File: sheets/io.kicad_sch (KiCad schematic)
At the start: 6 parts, among them Q5 BSS138, Q6 BSS138

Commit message: add mcu module + position components
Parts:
- removed Q5, Q6: BSS138, Package_TO_SOT_SMD:SOT-23, symbol Transistor_FET:BSS138
- added Q5, Q7: 2N7002, Package_TO_SOT_SMD:SOT-23, symbol Transistor_FET:2N7002
- added TB29, TB30: MKDSN 1,5/ 2-5,08, TerminalBlock_Phoenix:TerminalBlock_Phoenix_MKDS-1,5-2-5.08_1x02_P5.08mm_Horizontal, symbol Connector:Screw_Terminal_01x02
- renumbered R30 to R35, R31 to R36, R32 to R37, R33 to R38
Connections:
- net +3V3: now also Q5.1 (G), Q7.1 (G)
- net +5V: now also TB29.2 (Pin_2), TB30.1 (Pin_1), TB30.2 (Pin_2)
- net I2C.SCL: now also Q5.3 (D)
- net I2C.SDA: now also Q7.3 (D)
- net IO_SCL: now also Q5.2 (S)
- net IO_SDA: now also Q7.2 (S)
- new net +12V: TB29.1 (Pin_1)
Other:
- sheet Output PortC ports: added none; removed COMM[0..1], NC[0..7], NO[0..7]
- sheet Output PortD ports: added none; removed COMM[0..1], NC[0..7], NO[0..7]

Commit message: Updated MCU to MCU module + set SMD comp. footprints
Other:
- sheet Output PortC renamed OutputE
- sheet Output PortD renamed OutputF
- removed sheet IO PortA
- removed sheet IO PortB
- added sheet IO PortE (io-port.kicad_sch)
- added sheet IO PortF (io-port.kicad_sch)
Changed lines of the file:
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@@
 			(color 0 0 0 0.0000)
 		)
-		(property "Sheetname" "Output PortD"
+		(property "Sheetname" "OutputF"
 			(at 203.2 112.3184 0)
 			(effects
@@
 			(color 0 0 0 0.0000)
 		)
-		(property "Sheetname" "IO PortD"
+		(property "Sheetname" "IO PortF"
 			(at 113.03 109.7784 0)
 			(effects
@@
 			(color 0 0 0 0.0000)
 		)
-		(property "Sheetname" "Output PortC"
+		(property "Sheetname" "OutputE"
 			(at 203.2 93.2684 0)
 			(effects
@@
 			(color 0 0 0 0.0000)
 		)
-		(property "Sheetname" "IO PortC"
+		(property "Sheetname" "IO PortE"
 			(at 113.03 90.7284 0)
 			(effects
@@
 			(color 0 0 0 0.0000)
 		)
-		(property "Sheetname" "IO PortA"
+		(property "Sheetname" "IO PortC"
 			(at 113.03 52.6284 0)
 			(effects
@@
 			(color 0 0 0 0.0000)
 		)
-		(property "Sheetname" "IO PortB"
+		(property "Sheetname" "IO PortD"
 			(at 113.03 71.6784 0)
 			(effects

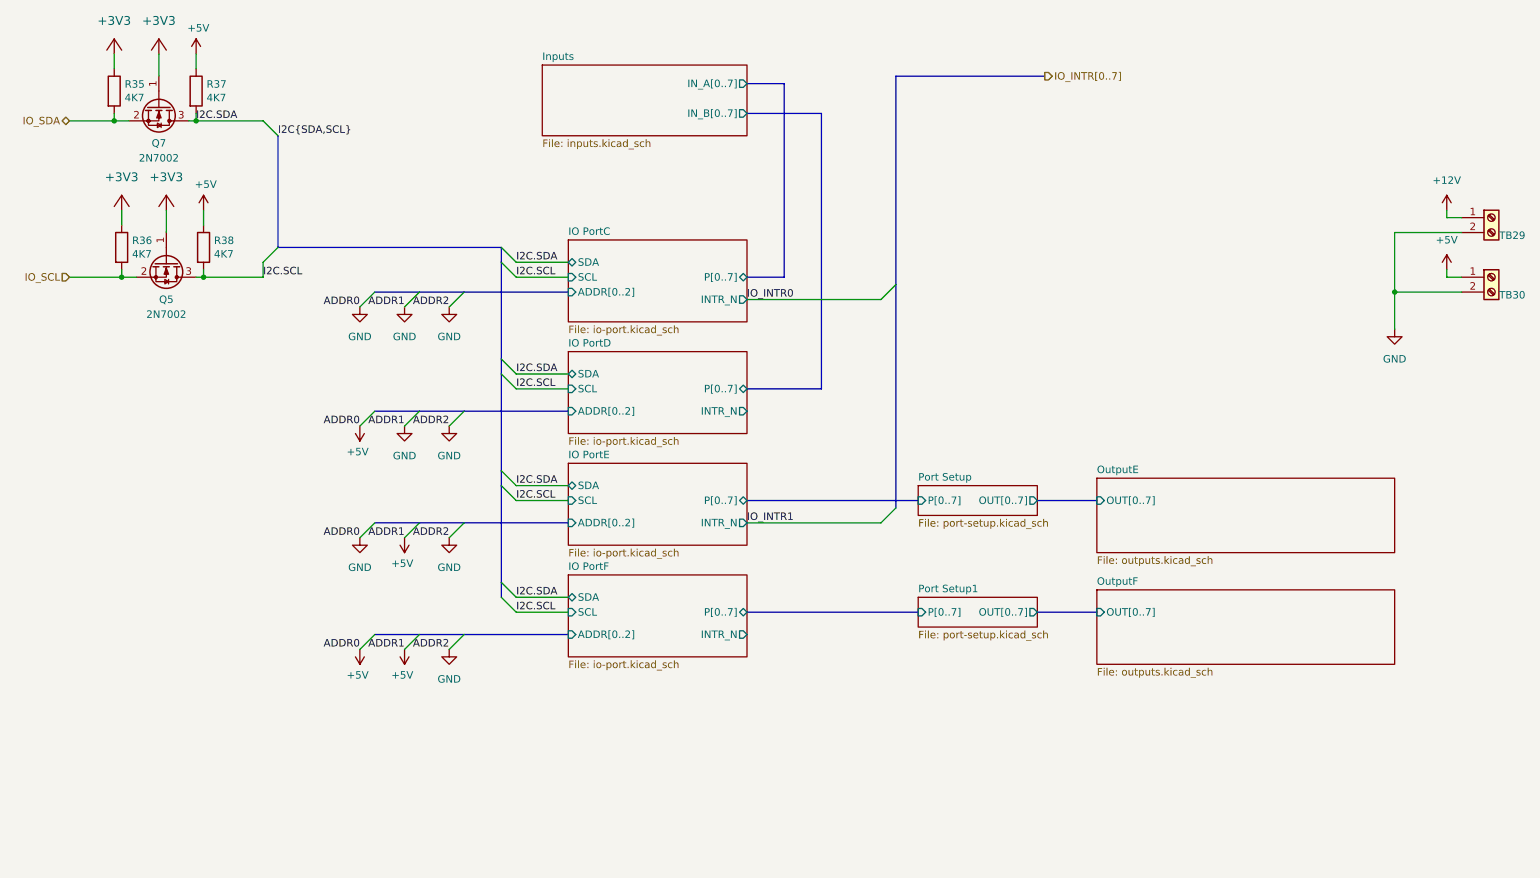
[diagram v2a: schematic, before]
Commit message: add PA an PB ports
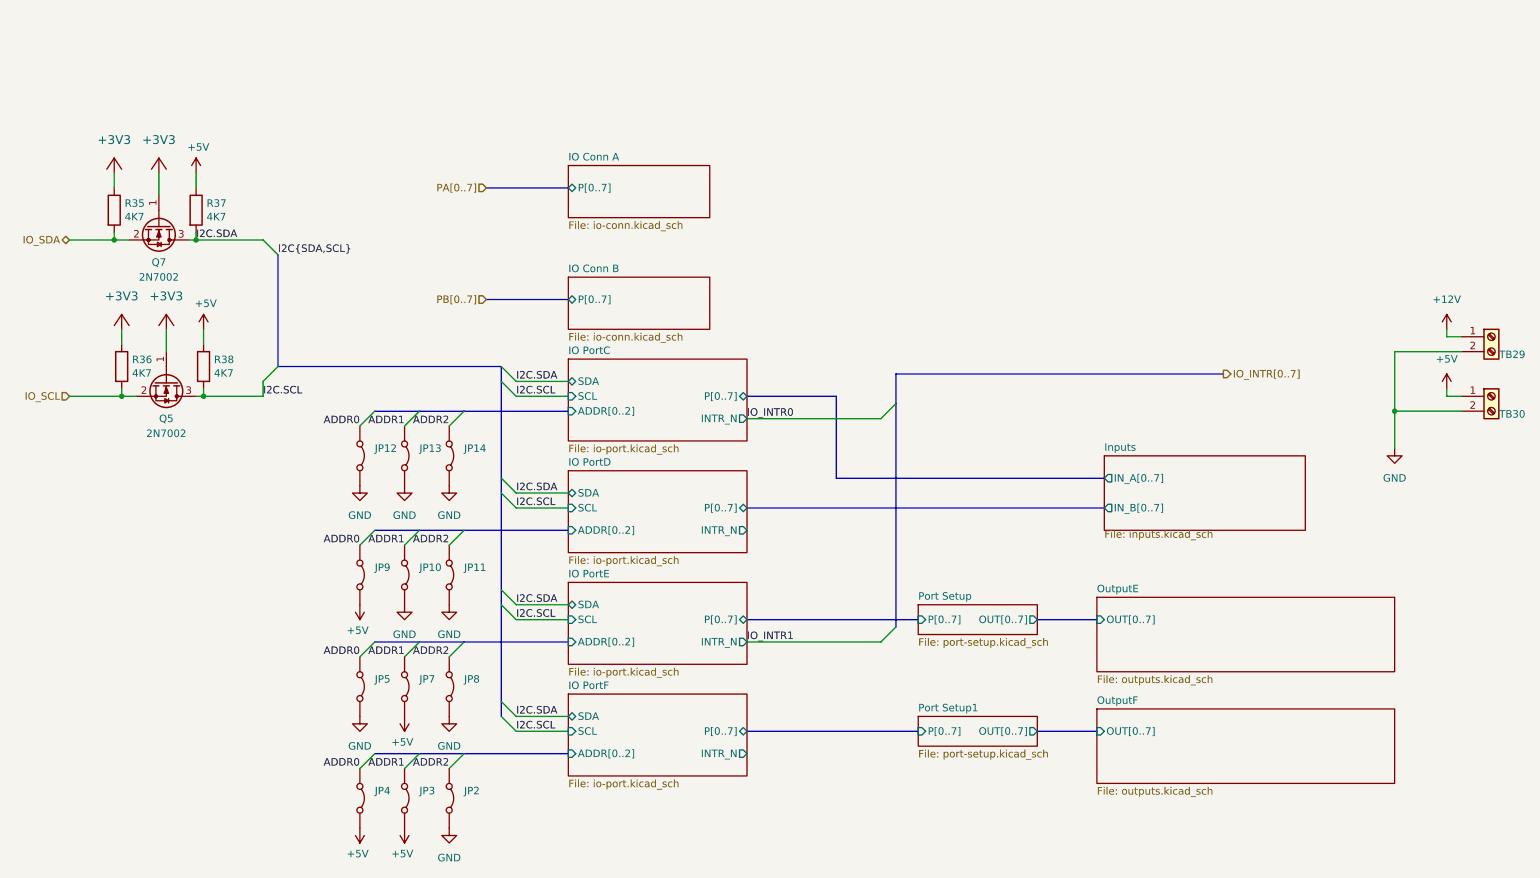
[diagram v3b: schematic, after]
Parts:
- added JP10, JP11, JP12, JP13, JP14, JP2, JP3, JP4, JP5, JP7, JP8, JP9: Jumper_2_Bridged, Jumper:SolderJumper-2_P1.3mm_Bridged_RoundedPad1.0x1.5mm, symbol Jumper:Jumper_2_Bridged
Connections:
- net +5V: now also JP3.1 (A), JP4.1 (A), JP7.1 (A), JP9.1 (A); no longer TB29.2 (Pin_2), TB30.2 (Pin_2)
- new net ADDR0: JP12.2 (B), JP4.2 (B), JP5.2 (B), JP9.2 (B)
- new net ADDR1: JP10.2 (B), JP13.2 (B), JP3.2 (B), JP7.2 (B)
- new net ADDR2: JP11.2 (B), JP14.2 (B), JP2.2 (B), JP8.2 (B)
- new net GND: JP10.1 (A), JP11.1 (A), JP12.1 (A), JP13.1 (A), JP14.1 (A), JP2.1 (A), JP5.1 (A), JP8.1 (A), TB29.2 (Pin_2), TB30.2 (Pin_2)
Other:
- added sheet IO Conn A (io-conn.kicad_sch)
- added sheet IO Conn B (io-conn.kicad_sch)
- moved on the sheet: Q5, Q7, R35, R36, R37, R38, TB29, TB30

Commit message: updated silk + started routing
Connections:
- removed net ADDR0: JP12.2 (B), JP4.2 (B), JP5.2 (B), JP9.2 (B)
- removed net ADDR1: JP10.2 (B), JP13.2 (B), JP3.2 (B), JP7.2 (B)
- removed net ADDR2: JP11.2 (B), JP14.2 (B), JP2.2 (B), JP8.2 (B)
- new net ADDRC0: JP12.2 (B)
- new net ADDRC1: JP13.2 (B)
- new net ADDRC2: JP14.2 (B)
- new net ADDRD0: JP9.2 (B)
- new net ADDRD1: JP10.2 (B)
- new net ADDRD2: JP11.2 (B)
- new net ADDRE0: JP5.2 (B)
- new net ADDRE1: JP7.2 (B)
- new net ADDRE2: JP8.2 (B)
- new net ADDRF0: JP4.2 (B)
- new net ADDRF1: JP3.2 (B)
- new net ADDRF2: JP2.2 (B)
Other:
- added sheet Port Setup2 (port-setup.kicad_sch)
- added sheet Port Setup3 (port-setup.kicad_sch)
